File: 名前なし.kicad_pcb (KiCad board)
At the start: 2 copper layers, 85 x 50 mm, 68 parts, among them IC1 SI8650AB-B-IS1, IC2 A3921KLPTR-T, IC3 SI8650AB-B-IS1, IC4 A3921KLPTR-T, J1 Conn_01x02, J2 Conn_01x03, J3 Conn_01x05, J4 Conn_01x02, J5 Bus_mechaken_PCIexpress_x16_1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, Q1 NVMFD5C446NT1G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

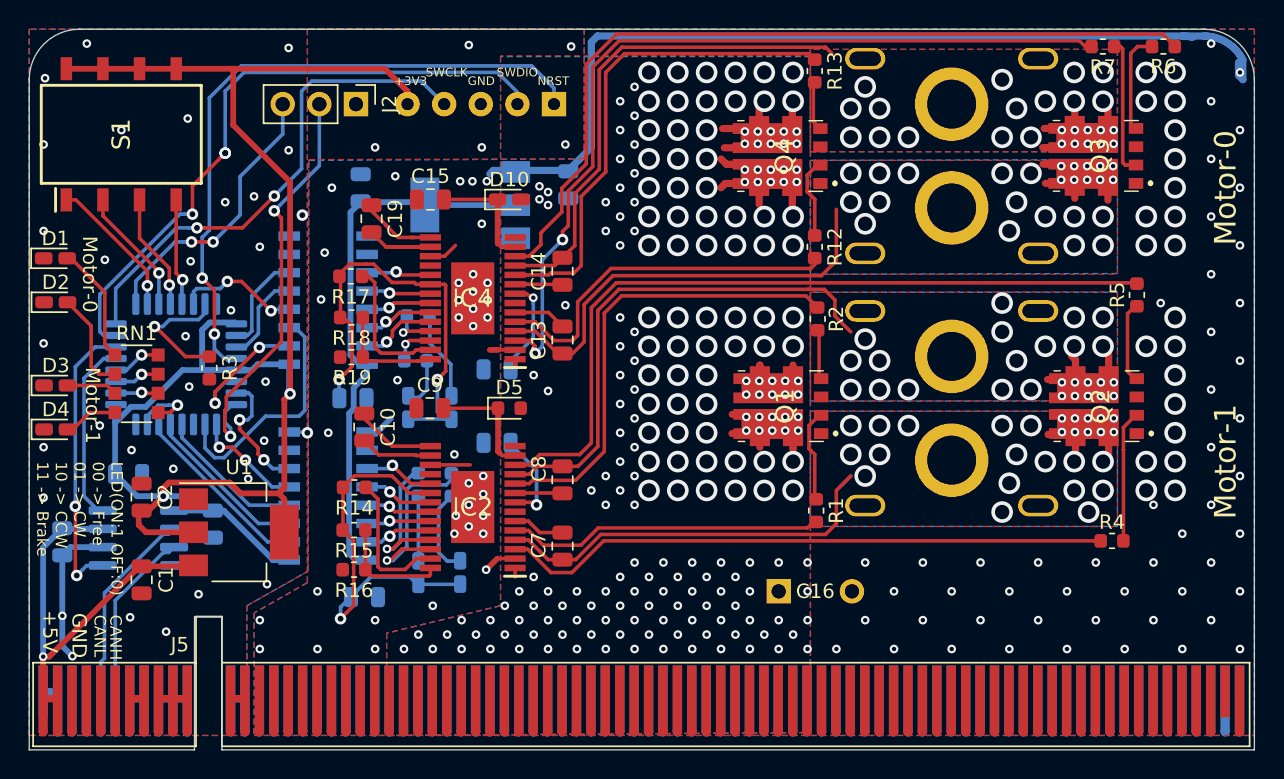
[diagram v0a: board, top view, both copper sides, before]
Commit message: change
放熱ビアを1mmに変更
その他大幅な変更
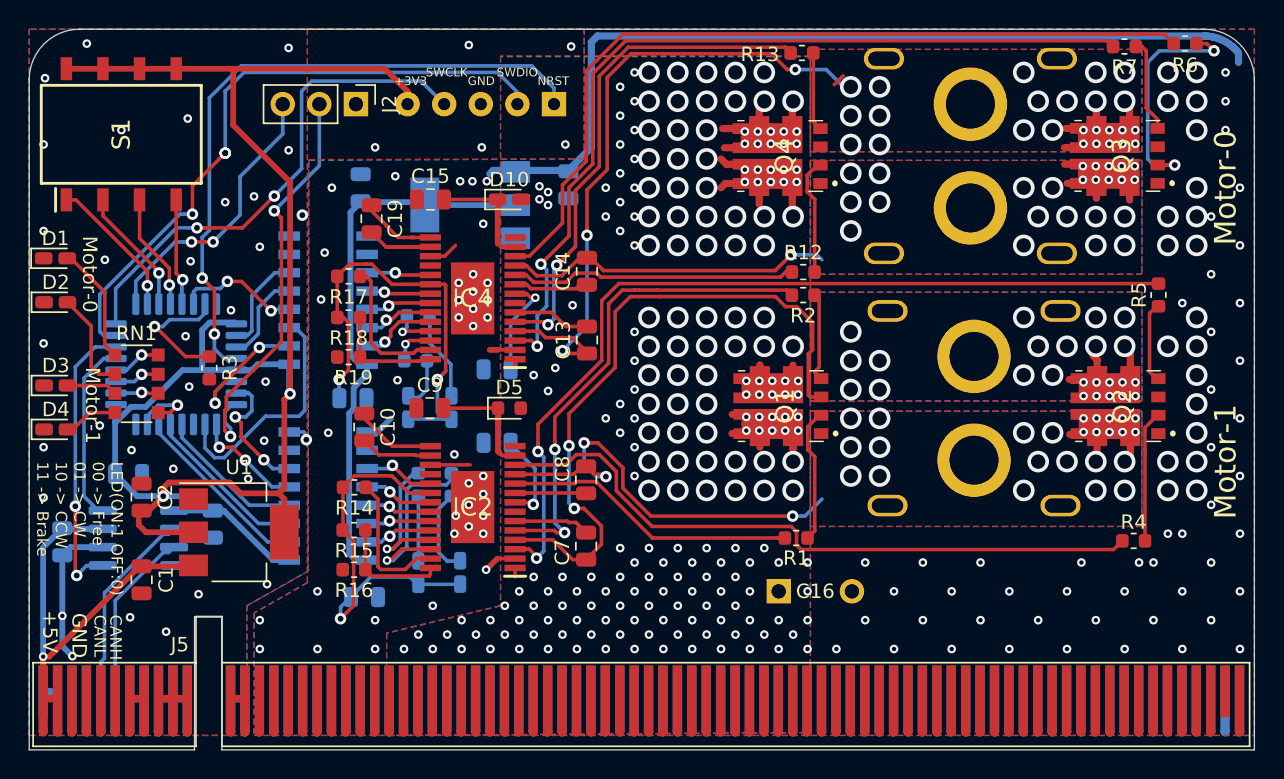
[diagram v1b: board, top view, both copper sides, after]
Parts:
- moved R1 2.35 mm to (103.2, 75.3), turned to 0 degrees
- moved R2 1.93 mm to (103.7, 58.5), turned to 180 degrees
- moved R12 1.92 mm to (103.7, 56.9), turned to 0 degrees
- moved C13 1.70 mm to (88.7, 61.6)
- moved C14 1.69 mm to (88.7, 56.8)
- moved C7 1.64 mm to (88.6, 75.9)
- moved C8 1.64 mm to (88.6, 71.3)
- moved J1 1.55 mm to (115.5, 66.3)
- moved R13 1.53 mm to (103.6, 41.6), turned to 180 degrees
- moved R6 1.51 mm to (130.2, 41.0), turned to 0 degrees
- moved Q2 1.50 mm to (125.8, 66.2)
- moved Q3 1.50 mm to (125.8, 48.8)
- moved R4 1.50 mm to (126.6, 75.5)
- moved R5 1.50 mm to (128.3, 58.4)
- moved R7 1.50 mm to (126.0, 41.2)
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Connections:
- J1 pad 1: SA_1 -> SB_1
- J1 pad 2: SB_1 -> SA_1
- J4 pad 1: SA_0 -> SB_0
- J4 pad 2: SB_0 -> SA_0
- Q1 pad 1: SB_1 -> SA_1
- Q1 pad 3: SA_1 -> SB_1
- Q2 pad 5: SA_1 -> SB_1
- Q2 pad 6: SB_1 -> SA_1
- Q3 pad 5: SA_0 -> SB_0
- Q3 pad 6: SB_0 -> SA_0
- Q4 pad 1: SB_0 -> SA_0
- Q4 pad 3: SA_0 -> SB_0
- R1 pad 1: GHB_1 -> GHA_1
- R12 pad 1: GHB_0 -> GHA_0
- R13 pad 2: GHA_0 -> GHB_0
- R2 pad 2: GHA_1 -> GHB_1
- R4 pad 1: GLB_1 -> GLA_1
- R5 pad 2: GLA_1 -> GLB_1
- R6 pad 2: Net-(Q3-Pad4) -> Net-(Q3-Pad2)
- R7 pad 1: Net-(Q3-Pad2) -> Net-(Q3-Pad4)
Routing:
- net SB_1: track 36.0 -> 54.9 mm, vias 27 -> 26
- net GLB_1: track 42.6 -> 61.0 mm, vias 0 -> 2
- net SB_0: track 34.7 -> 52.7 mm, vias 25 -> 28
- net GHA_0: track 34.2 -> 19.9 mm
- net SA_0: track 40.4 -> 26.9 mm
- net GHB_1: track 21.8 -> 34.6 mm, vias 0 -> 2
- net GHA_1: track 32.3 -> 20.4 mm
- net GHB_0: track 25.3 -> 35.3 mm, vias 0 -> 2
- net GLA_1: track 53.9 -> 46.7 mm
- net Net-(Q3-Pad2): track 9.55 -> 16.4 mm, vias 0 -> 2
- net SA_1: track 44.1 -> 37.4 mm, vias 26 -> 28
- net Net-(Q1-Pad4): track 3.46 -> 7.29 mm
- net GNDPWR: track 75.6 -> 72.3 mm, vias 109 -> 106
- net Net-(Q1-Pad2): track 6.44 -> 9.42 mm
- net Net-(Q4-Pad2): track 5.61 -> 8.15 mm
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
